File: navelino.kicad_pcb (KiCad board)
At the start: 2 copper layers, 45.6 x 37.3 mm, 67 parts, among them IC1 ATMEGA328P-A, P3 CONN_6, SW1 SW_PUSH, SW2 SW_PUSH, U1 CJA1117B-3.3

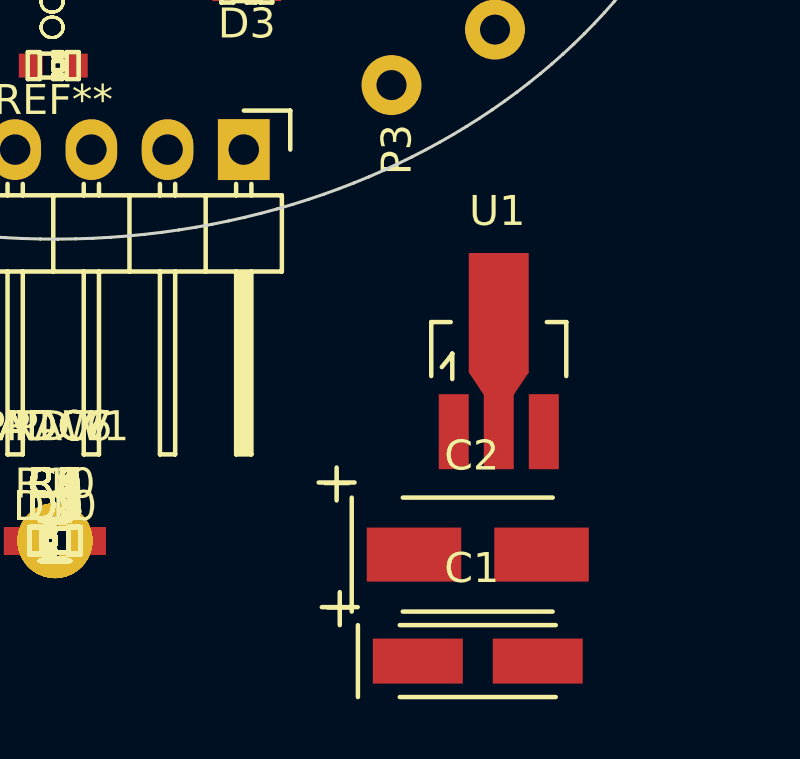
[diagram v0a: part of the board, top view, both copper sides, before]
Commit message: Actualizado el regulador a algo más pequeño :)
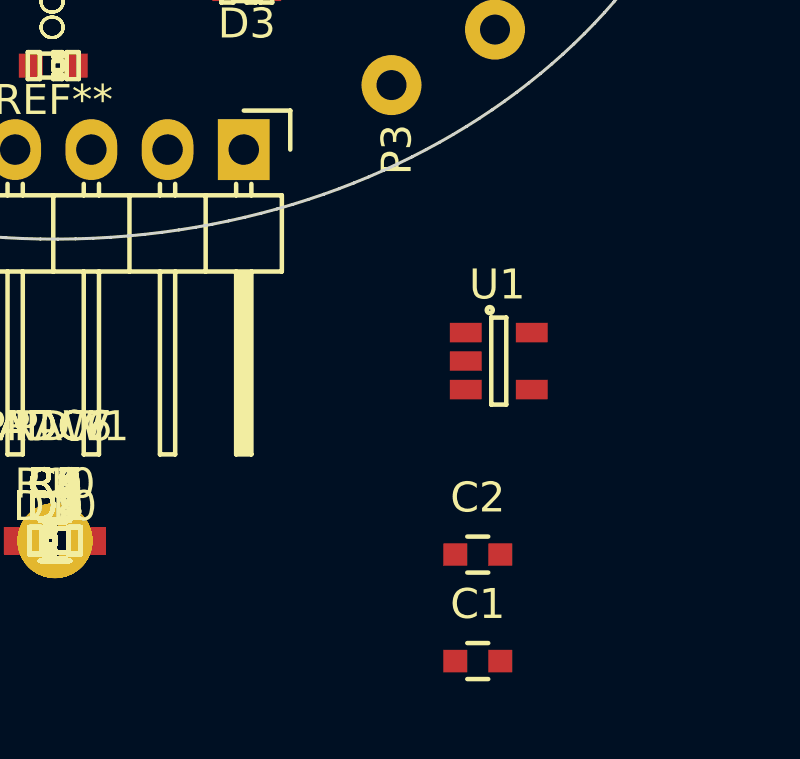
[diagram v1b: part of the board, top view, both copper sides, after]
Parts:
- C1: value 10uF -> 0.1uF; footprint Capacitors_Tantalum_SMD:TantalC_SizeA_EIA-3216_HandSoldering -> Capacitors_SMD:C_0603
- C2: value 22uF -> 1uF; footprint Capacitors_Tantalum_SMD:TantalC_SizeB_EIA-3528_HandSoldering -> Capacitors_SMD:C_0603
- C4: value C -> 0.1uF
- U1: value CJA1117B-3.3 -> XC6204B332MR; footprint Housings_SOT-89:SOT89-3_Housing_Handsoldering -> Housings_SOT-23_SOT-143_TSOT-6:SOT-23-5
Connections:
- U1 pad 1: GND -> RAW
- U1 pad 2: VCC -> GND

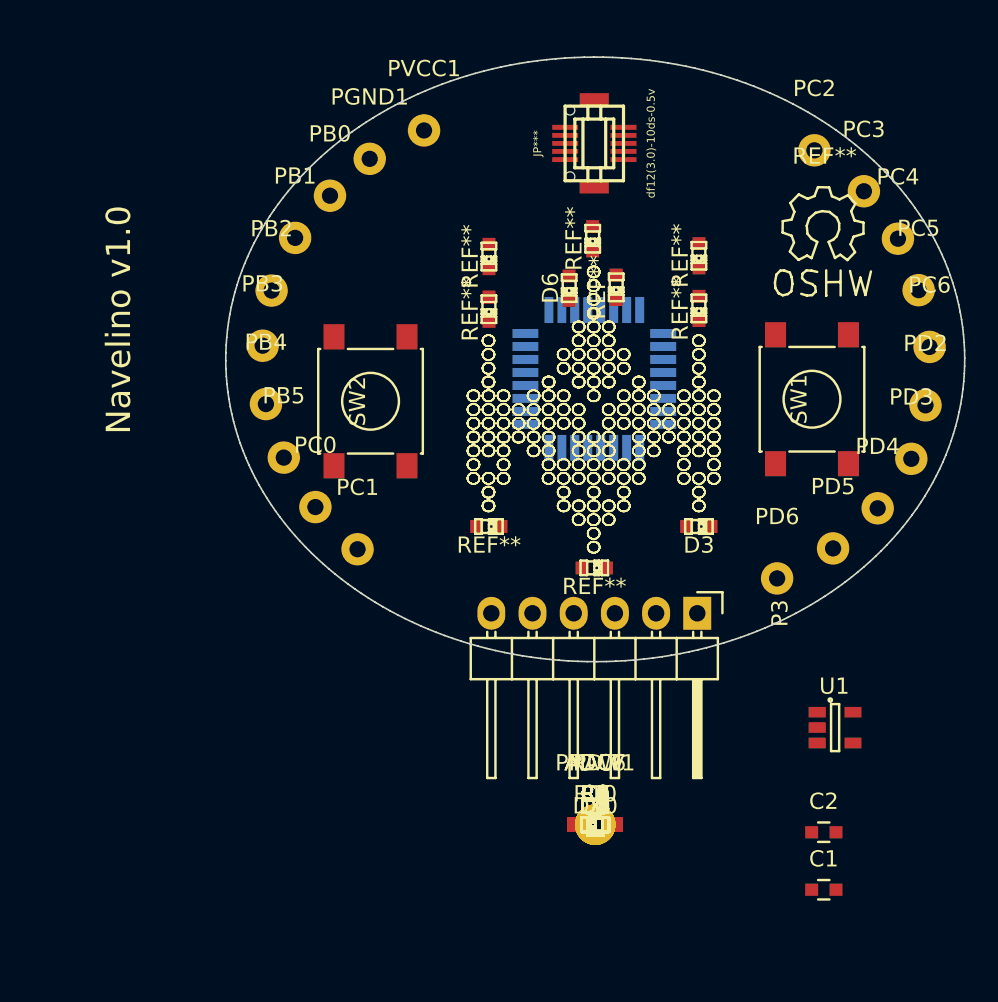
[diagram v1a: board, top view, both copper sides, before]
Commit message: Cambiados casi todos los componentes de 06 a 08 para que pueda funcionar como taller de soldadura SMD Añadido el Jumper para poder desactivar los leds y usar los pines libremente
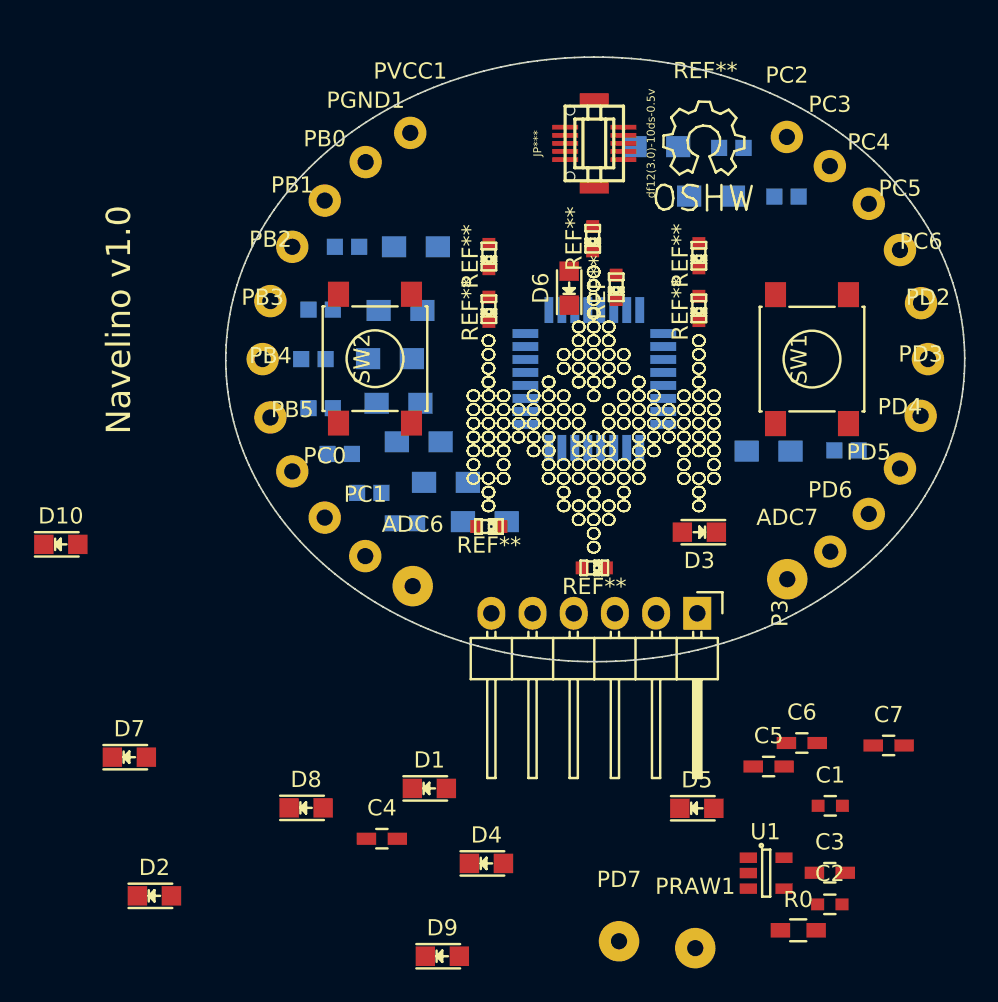
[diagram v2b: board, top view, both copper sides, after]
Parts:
- added JP1: JUMPER, tmw:PCB_JUMPER, B.Cu at (109.8, 122.3)
- added JP10: JUMPER, tmw:PCB_JUMPER, B.Cu at (140.6, 134.8)
- added JP2: JUMPER, tmw:PCB_JUMPER, B.Cu at (108.1, 126.2)
- added JP3: JUMPER, tmw:PCB_JUMPER, B.Cu at (107.7, 129.2)
- added JP4: JUMPER, tmw:PCB_JUMPER, B.Cu at (108.1, 132.2)
- added JP5: JUMPER, tmw:PCB_JUMPER, B.Cu at (109.3, 135.1)
- added JP6: JUMPER, tmw:PCB_JUMPER, B.Cu at (111.1, 137.5)
- added JP7: JUMPER, tmw:PCB_JUMPER, B.Cu at (113.3, 139.3)
- added JP8: JUMPER, tmw:PCB_JUMPER, B.Cu at (133.4, 116.2)
- added JP9: JUMPER, tmw:PCB_JUMPER, B.Cu at (136.8, 119.2)
- D1, D10, D2, D3, D4, D5, D6, D7, D8, D9: footprint LEDs:LED-0603 -> LEDs:LED-0805
- R1, R10, R2, R3, R4, R5, R6, R7, R8, R9: footprint Resistors_SMD:R_0603_HandSoldering -> Resistors_SMD:R_0805_HandSoldering; moved to B.Cu
- moved R8 42.0 mm to (128.8, 116.1), turned to 180 degrees
- moved R9 39.4 mm to (132.2, 119.2), turned to 180 degrees
- moved R1 37.3 mm to (114.0, 122.3)
- moved D10 37.2 mm to (92.1, 140.7)
- moved R2 33.9 mm to (113.0, 126.2)
- moved R3 31.4 mm to (112.4, 129.2)
- moved D7 29.0 mm to (96.3, 153.8)
- moved R4 28.7 mm to (112.9, 131.9)
- moved D2 27.5 mm to (97.9, 162.3)
- moved R5 26.0 mm to (114.2, 134.3)
- moved R10 25.4 mm to (135.8, 134.9), turned to 180 degrees
- moved R6 23.0 mm to (115.8, 136.8)
- moved R7 19.9 mm to (118.2, 139.2)
- moved ADC7 19.2 mm to (136.9, 142.8)
- moved C7 18.7 mm to (143.2, 153.1)
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
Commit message: Finalizado el routing!
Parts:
- removed JP***: df12(3.0)-10ds-0.5v, w_conn_df12:df12(3.0)-10ds-0.5v
- removed REF** (x8): LED-0603, LEDs:LED-0603
- removed REF**: Symbol_OSHW-Logo_SilkScreen, Symbols:Symbol_OSHW-Logo_SilkScreen
- added CON1: USB-MINI-B, ST-USB-001G, B.Cu at (125.0, 115.5)
- added P1: CONN_5X2, SEEED:df12(3.0)-10ds-0.5v, F.Cu at (125.0, 114.2)
- added SW0: SW_PUSH, SEEED:B3U-1000P, B.Cu at (132.6, 140.0)
- added X0: CRYSTAL, SMD-CRYSTAL-8MHZ-20PF-20PPM_2P-5.0X3.2MM_:X2-SMD-5.0X3.2X1.3MM, B.Cu at (120.4, 140.0)
- C1, C2: footprint Capacitors_SMD:C_0603 -> Capacitors_SMD:C_0805; moved to B.Cu
- C3, C4, C5, C6, C7: footprint Capacitors_SMD:C_0603_HandSoldering -> Capacitors_SMD:C_0805; moved to B.Cu
- D1: renamed from D10; value LED -> BLUE
- D10: renamed from D1; value BLUE -> LED
- D2: renamed from D5; value LED -> BLUE
- D3: renamed from D9; value LED -> BLUE
- D5: renamed from D2; value BLUE -> LED
- D8: renamed from D3; value BLUE -> LED
- JP1, JP10, JP2, JP3, JP4, JP5, JP6, JP7, JP8, JP9: footprint tmw:PCB_JUMPER -> Wire_Connections_Bridges:PCB_JUMPER
- R0: footprint Resistors_SMD:R_0603_HandSoldering -> Resistors_SMD:R_0805_HandSoldering; moved to B.Cu
- SW1, SW2: value SW_PUSH -> SMD-SWITCH-TACTILE-SPST-NO(4P-D6.0MM); footprint Buttons_Switches_SMD:SW_SPST_PTS645 -> SEEED:SW4-SMD-6.0X6.0X5.0MM
- U1: footprint Housings_SOT-23_SOT-143_TSOT-6:SOT-23-5 -> TO_SOT_Packages_SMD:SOT-23-5; moved to B.Cu
- moved PRAW1 52.6 mm to (110.9, 117.1)
- moved C2 44.9 mm to (128.1, 119.5), turned to 270 degrees
- moved D1 43.7 mm to (131.4, 121.5), turned to 270 degrees
- moved U1 42.8 mm to (125.0, 119.5), turned to 90 degrees
- moved D6 41.5 mm to (125.0, 119.4), turned to 270 degrees
- moved C1 41.3 mm to (121.9, 119.5), turned to 90 degrees
- moved D3 40.5 mm to (118.5, 125.6), turned to 90 degrees
- moved C3 39.8 mm to (125.0, 123.8)
- moved D7 39.2 mm to (118.5, 121.4), turned to 270 degrees
- moved D4 37.1 mm to (123.4, 123.6), turned to 90 degrees
- moved C7 36.4 mm to (119.1, 125.7), turned to 180 degrees
- moved JP2 34.4 mm to (142.4, 129.2), turned to 180 degrees
- moved JP1 32.4 mm to (141.9, 126.2), turned to 180 degrees
- moved D2 31.3 mm to (131.4, 125.6), turned to 90 degrees
- moved D5 30.5 mm to (118.4, 139.7)
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- renumbered D8 to D6, D6 to D9
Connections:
- D1 pad 1: Net-(D10-Pad1) -> Net-(D1-Pad1)
- D10 pad 1: Net-(D1-Pad1) -> Net-(D10-Pad1)
- D2 pad 1: Net-(D5-Pad1) -> Net-(D2-Pad1)
- D3 pad 1: Net-(D9-Pad1) -> Net-(D3-Pad1)
- D5 pad 1: Net-(D2-Pad1) -> Net-(D5-Pad1)
- D6 pad 1: Net-(D8-Pad1) -> Net-(D6-Pad1)
- D8 pad 1: Net-(D3-Pad1) -> Net-(D8-Pad1)
- D9 pad 1: Net-(D6-Pad1) -> Net-(D9-Pad1)
- JP1 pad 1: PB1 -> PD2
- JP2 pad 1: PB2 -> PD3
- JP3 pad 1: PB3 -> PB3/MOSI
- JP4 pad 1: PB4 -> PB4/MISO
- JP5 pad 1: SCK/PB5 -> PB5/SCK
- JP6 pad 1: PC0 -> PB1
- JP7 pad 1: PC1 -> PB2
- JP8 pad 1: PC2 -> PD5
- PB3 pad 1: PB3 -> PB3/MOSI
- PB4 pad 1: PB4 -> PB4/MISO
- PB5 pad 1: SCK/PB5 -> PB5/SCK
- SW1 pad 1: PB0 -> PC2
- SW1 pad 2: GND -> Net-(SW1-Pad2)
- SW2 pad 1: PD5 -> PB0
- SW2 pad 2: GND -> Net-(SW2-Pad2)
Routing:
- net GND: track 0.00 -> 138.8 mm, vias 0 -> 10
- net VCC: track 0.00 -> 73.7 mm, vias 0 -> 5
- net RESET: track 0.00 -> 60.1 mm, vias 0 -> 8
- net PB3/MOSI: track 0.00 -> 39.2 mm, vias 0 -> 5
- net PB5/SCK: track 0.00 -> 38.9 mm, vias 0 -> 4
- net PB4/MISO: track 0.00 -> 37.9 mm, vias 0 -> 3
- net PD7: track 0.00 -> 32.5 mm, vias 0 -> 2
- net PD6: track 0.00 -> 31.0 mm, vias 0 -> 2
- net PD5: track 0.00 -> 30.0 mm
- net PB0: track 0.00 -> 29.4 mm, vias 0 -> 1
- net RAW: track 0.00 -> 25.7 mm, vias 0 -> 4
- net PC0: track 0.00 -> 24.9 mm, vias 0 -> 1
- net PC1: track 0.00 -> 24.4 mm, vias 0 -> 1
- net A6: track 0.00 -> 24.3 mm, vias 0 -> 1
- net A7: track 0.00 -> 24.2 mm, vias 0 -> 1
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
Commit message: Un poco de amor para el Silkscreen
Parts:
- CON1: value USB-MINI-B -> USB
- renumbered PB2 to 10, PB3 to 11, PB4 to 12, PB5 to 13, PD2 to 2, PD3 to 3, PD4 to 4, PD5 to 5, PD6 to 6, PD7 to 7, PB0 to 8, PB1 to 9, PC0 to A0, PC1 to A1, PC2 to A2, PC3 to A3, PC4 to A4, PC5 to A5, ADC6 to A6, ADC7 to A7, PGND1 to GND, PRAW1 to RAW, PC6 to RESET, PVCC1 to VCC
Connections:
- CON1 pad 6: Net-(CON1-Pad6) -> (no net)
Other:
- board text added: "Hacker SpaceVLC"
